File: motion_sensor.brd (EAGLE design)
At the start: 30 x 30 mm, 45 parts, among them J1 AVR_SPI_PRG_6PTH, U1 LP2985A-33DBVTE4, U2 nRF8001, U3 ATMEGA328P_TQFP, Y1 16MHz, Y2 FC-255 32.7680K-A3, Y4 16MHz

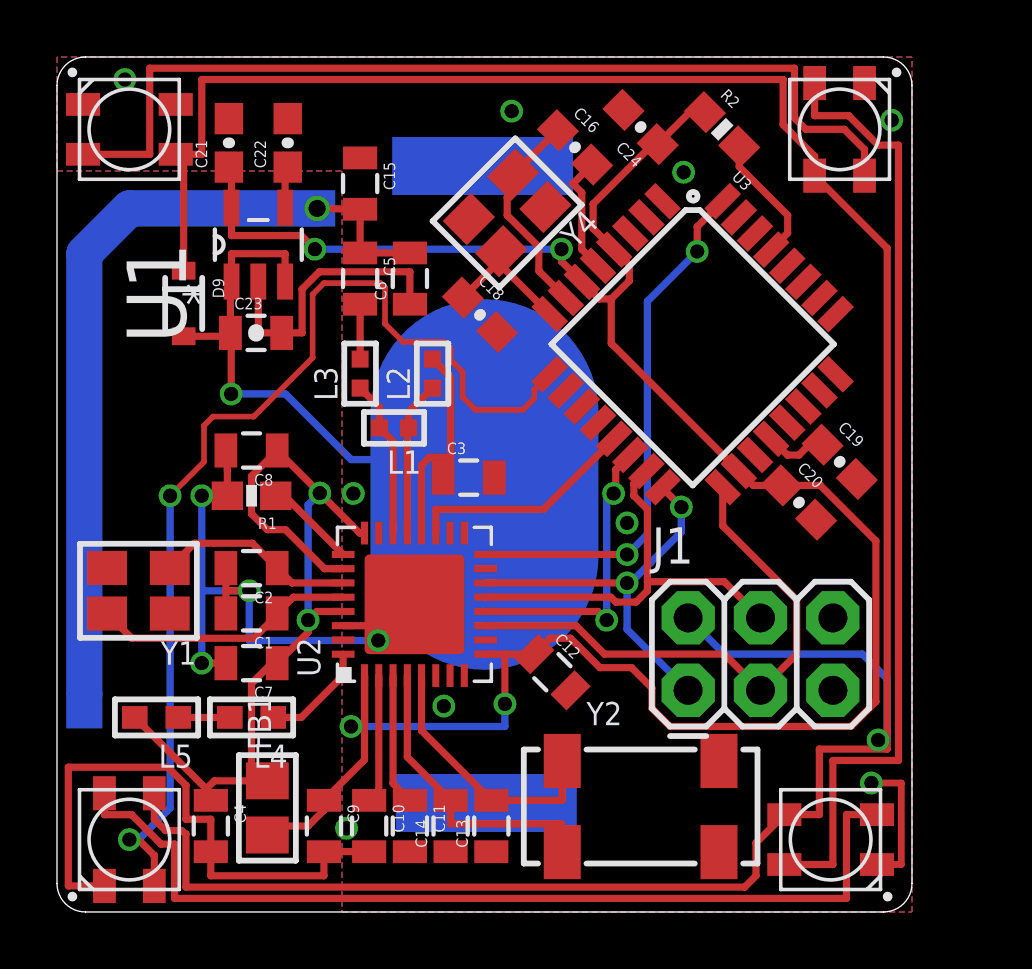
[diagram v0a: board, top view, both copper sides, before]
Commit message: Fixing bug with reset circuit. Add FTDI header.
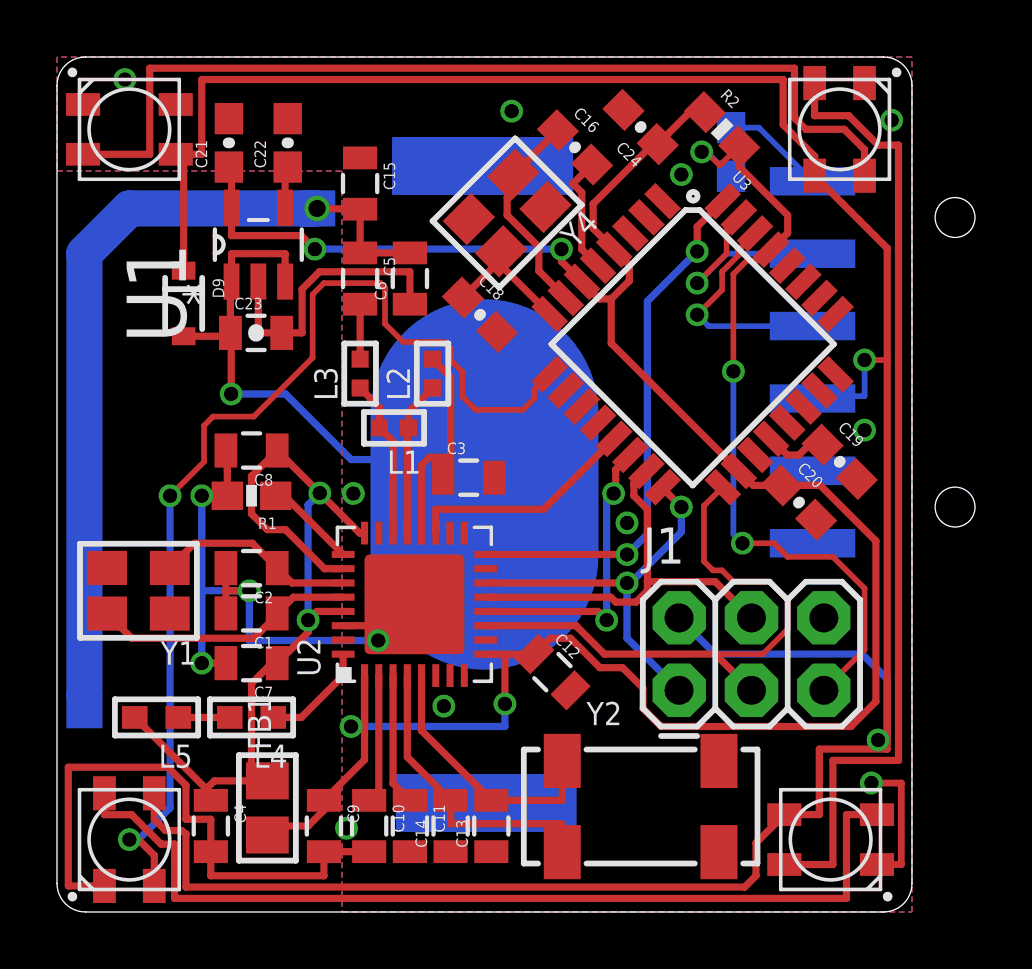
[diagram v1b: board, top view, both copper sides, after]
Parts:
- added C17: 0.1uF, SparkFun-Capacitors:0603-CAP
- added J2: FTDI_DEVICERA_SMT, SparkFun-Connectors:FTDI_DEVICE_RA_SMT
- moved J1 0.32 mm to (21.8, 7.78)
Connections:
- removed net N$26: R2.2, U3.29
- new net DTR: C17.2, J2.1
- net 5V: now also J2.4
- net GND: now also J2.5, J2.6
- net RESET: now also C17.1, R2.2, U3.29
- net RX: now also J2.3
- net TX: now also J2.2
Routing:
- net RESET: track 0.00 -> 28.1 mm, vias 0 -> 3
- net RX: track 0.00 -> 7.91 mm, vias 0 -> 1
- net TX: track 0.00 -> 7.39 mm, vias 0 -> 1
- net N$26: track 4.57 -> 0.00 mm
- net 5V: track 96.7 -> 100.9 mm, vias 1 -> 2
- net DTR: track 0.00 -> 3.64 mm
- net SCK: track 19.3 -> 20.6 mm
- net GND: vias 13 -> 14
